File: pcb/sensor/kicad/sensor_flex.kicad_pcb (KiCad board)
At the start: 2 copper layers, 195.7 x 8.4 mm, 8 parts, among them J1 CN2 mate (TBD), J2 S7081-42R +5V, J3 S7081-42R GND, U1 SHT45

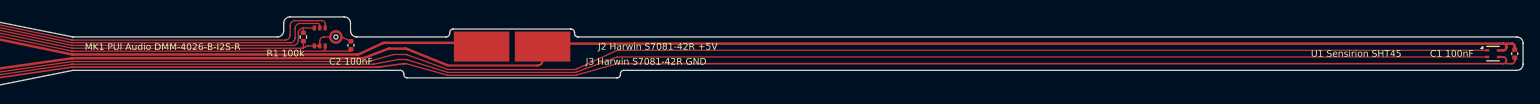
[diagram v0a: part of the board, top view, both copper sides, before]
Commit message: Back cover: snap hooks for the flex, stronger magnet clips, rounded contact posts; #6 countersink and PLATE_Y on the trim
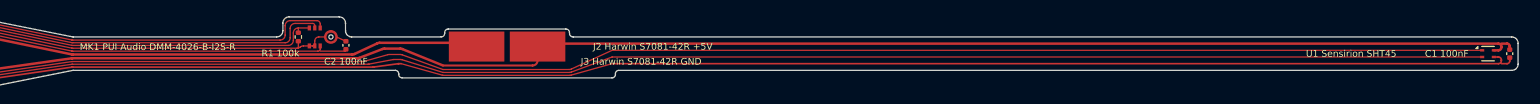
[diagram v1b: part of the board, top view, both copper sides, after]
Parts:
- moved C1 0.60 mm to (288.1, 100.0)
- moved U1 0.60 mm to (285.5, 100.0)
- moved C2 0.60 mm to (148.7, 99.0)
- moved J2 0.60 mm to (164.3, 99.2)
- moved J3 0.60 mm to (171.6, 99.2)
- moved MK1 0.60 mm to (145.9, 98.0)
- moved R1 0.60 mm to (143.0, 98.0)
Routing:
- net GND: track 188.1 -> 187.5 mm
- net +3V3: track 191.4 -> 190.8 mm
- net /SCL: track 185.6 -> 185.0 mm
- net /SDA: track 185.2 -> 184.6 mm
- net /MIC_3V3: track 48.9 -> 48.3 mm
- net /I2S_WS: track 50.6 -> 50.0 mm
- net /I2S_SCK: track 48.9 -> 48.3 mm
- net +5V: track 60.6 -> 60.0 mm
- net /MIC_GND: track 49.4 -> 48.8 mm
- net /I2S_SD: track 47.5 -> 46.9 mm
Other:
- board size 195.7 x 8.4 mm -> 195.1 x 8.4 mm

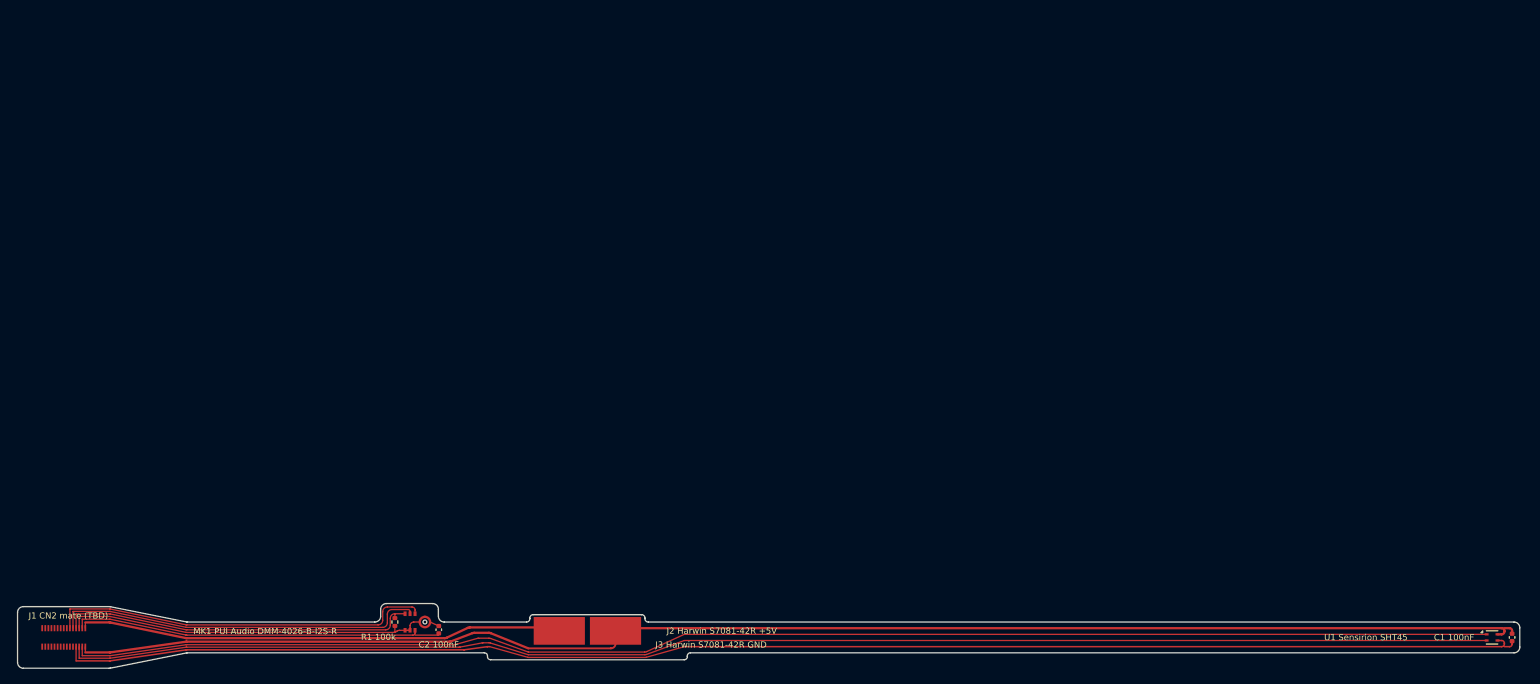
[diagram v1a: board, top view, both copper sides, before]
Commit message: Smaller plate, flex ramps and tape points, battery-free tongue on the sensor flex, back cover hooks
- Plate 72 x 132, 5 V contact in the corner, band groove, microphone below the band, two-layer
  sensor flex (D-47)
- Ramps over the flex slopes; tape geometry and tape renders (render_tape.py, D-48)
- Battery-free tongue moved from the 5 V jumper to the sensor flex: under the trim's tab and strip,
  under the floor insert, which hangs from the strip; EU tongue under its floor insert (D-49)
- Back cover: bottom latch 2.9 mm from the edge, end-section snap hooks, notch for the run under
  the GND block; plate clips kept for PETG
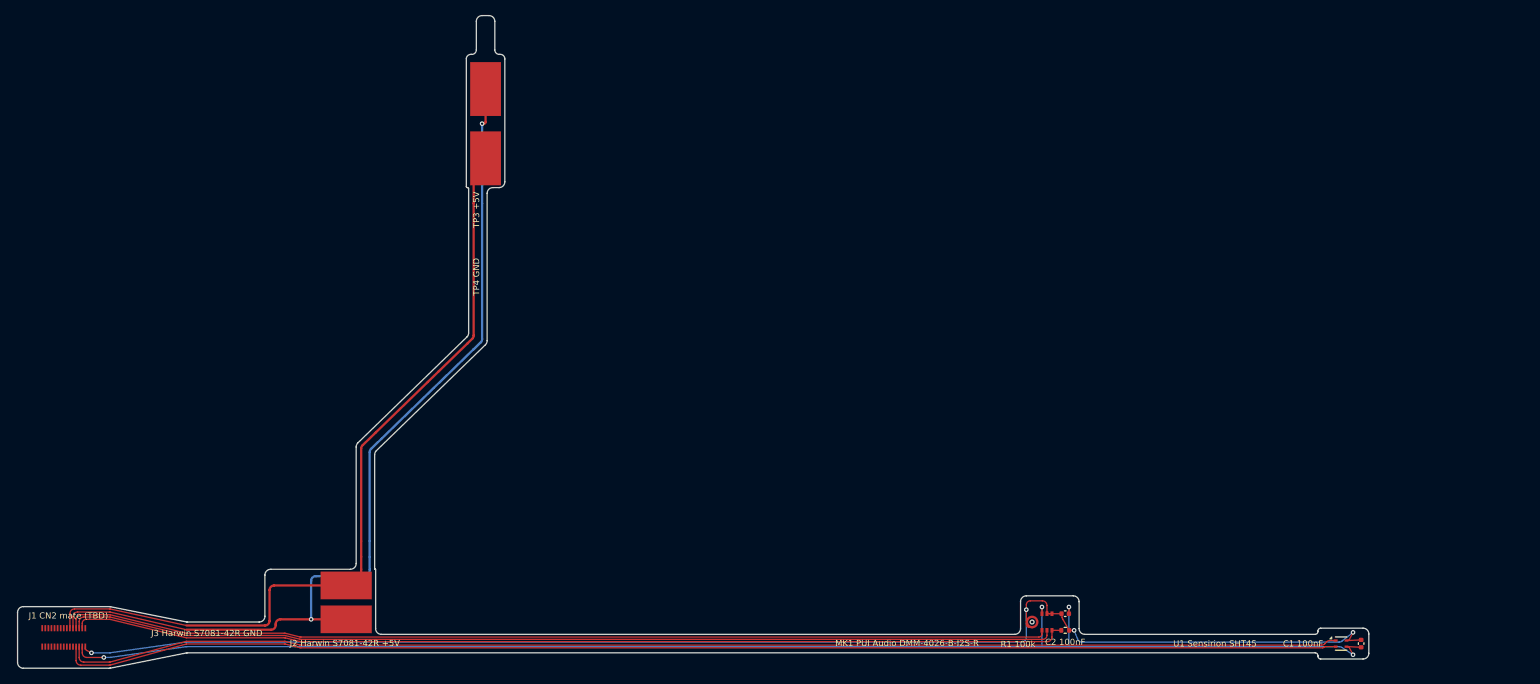
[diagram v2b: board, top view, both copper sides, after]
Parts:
- added TP3: +5V floor pad, sensor:Contact_Pad_7x4mm, F.Cu at (154.8, 37.8)
- added TP4: GND floor pad, sensor:Contact_Pad_7x4mm, F.Cu at (154.8, 28.8)
- moved R1 87.1 mm to (230.0, 99.1), turned to 0 degrees
- moved C2 81.4 mm to (230.0, 96.9), turned to 0 degrees
- moved MK1 80.8 mm to (226.7, 98.0), turned to -90 degrees
- moved J3 35.0 mm to (136.7, 97.7)
- moved J2 28.3 mm to (136.7, 93.2)
- moved C1 19.6 mm to (268.5, 100.8)
- moved U1 19.6 mm to (265.9, 100.8)
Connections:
- C1 pad 2: GND -> /GND_SENS
- C2 pad 1: /MIC_3V3 -> /GND_SENS
- C2 pad 2: /MIC_GND -> +3V3
- J1 pad 19: /I2S_WS -> +5V
- J1 pad 21: /I2S_SCK -> GND
- J1 pad 23: /I2S_SD -> /I2S_WS
- J1 pad 24: +3V3 -> /SCL
- J1 pad 25: /MIC_GND -> /I2S_SCK
- J1 pad 26: /SCL -> /SDA
- J1 pad 27: /MIC_3V3 -> /I2S_SD
- J1 pad 28: /SDA -> +3V3
- J1 pad 29: +5V -> unconnected-(J1-Pin_29-Pad29)
- J1 pad 30: GND -> /GND_SENS
- MK1 pad 1: /MIC_GND -> /GND_SENS
- MK1 pad 2: /MIC_GND -> /GND_SENS
- MK1 pad 3: /MIC_3V3 -> +3V3
- MK1 pad 4: /MIC_GND -> /GND_SENS
- R1 pad 2: /MIC_GND -> /GND_SENS
- U1 pad 4: GND -> /GND_SENS
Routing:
- net /GND_SENS: track 0.00 -> 179.9 mm, vias 0 -> 4
- net /I2S_SD: track 46.9 -> 129.6 mm
- net /I2S_SCK: track 48.3 -> 128.1 mm
- net /I2S_WS: track 50.0 -> 127.9 mm
- net GND: track 187.5 -> 120.8 mm, vias 0 -> 2
- net /MIC_GND: track 48.8 -> 0.00 mm
- net /MIC_3V3: track 48.3 -> 0.00 mm
- net +5V: track 60.0 -> 104.5 mm
- net /SDA: track 184.6 -> 165.5 mm
- net /SCL: track 185.0 -> 166.2 mm
- net +3V3: track 190.8 -> 181.6 mm, vias 0 -> 4
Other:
- board size 195.1 x 8.4 mm -> 175.5 x 84.7 mm
- board text added: "STIFFENER FR4 0.1 mm, back side"
- board text added: "TONGUE FOLD: 45 deg, flips the strip"
- board text added: "TP3 +5V"
- board text added: "TP4 GND"
